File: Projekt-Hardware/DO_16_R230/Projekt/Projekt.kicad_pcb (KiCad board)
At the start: 2 copper layers, 38 parts, among them J1 COM_Bus, J2 COM_Bus, K1 DIPxx-1Cxx-51x, K10 DIPxx-1Cxx-51x, K11 DIPxx-1Cxx-51x, K12 DIPxx-1Cxx-51x, K13 DIPxx-1Cxx-51x, K14 DIPxx-1Cxx-51x, K15 DIPxx-1Cxx-51x, K16 DIPxx-1Cxx-51x, K2 DIPxx-1Cxx-51x, K3 DIPxx-1Cxx-51x, K4 DIPxx-1Cxx-51x, K5 DIPxx-1Cxx-51x, K6 DIPxx-1Cxx-51x, K7 DIPxx-1Cxx-51x, K8 DIPxx-1Cxx-51x, K9 DIPxx-1Cxx-51x, U1 ATmega328P-PU, X1 DO 16-2

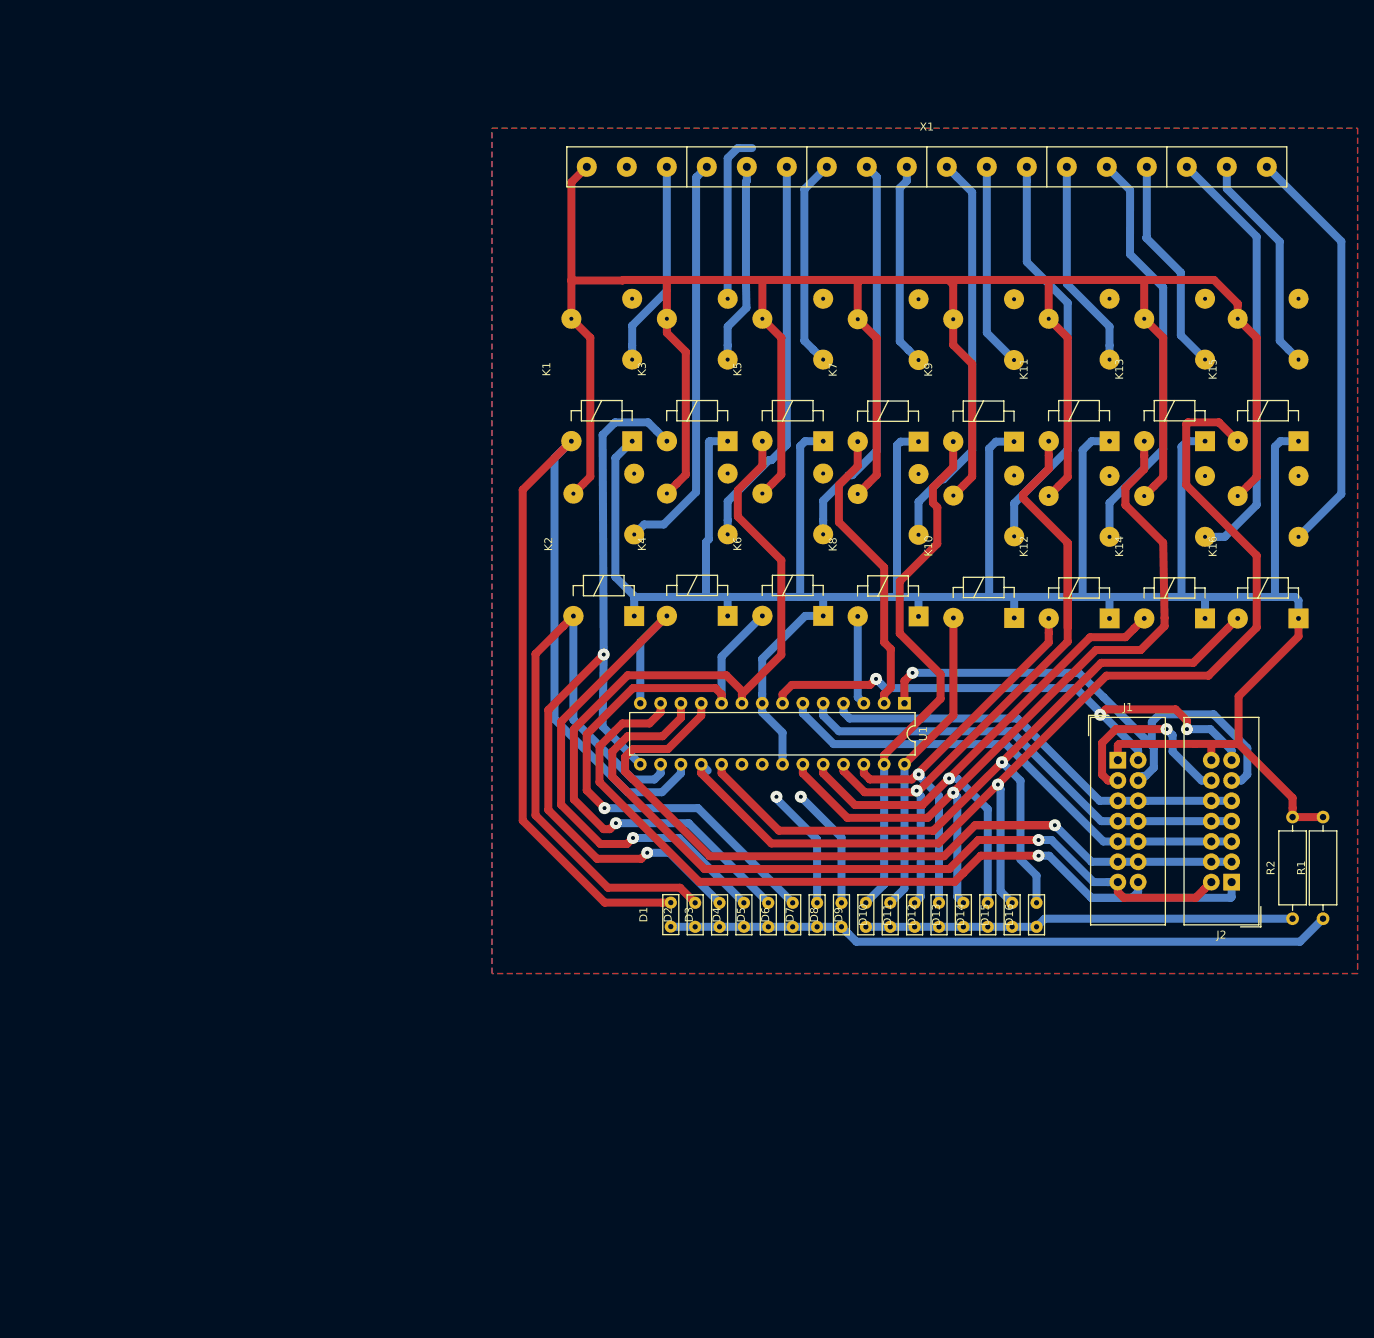
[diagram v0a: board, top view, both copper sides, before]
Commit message: Erster (meschanischer) Entwurf für DO_16_R230 Modul
Erster Entwurf für meschanische Bauteile des
DO_16_R230 Moduls:
- Entwurf für Leiterplatten
Fehlende Entwürfe:
- Gehäuse
- Halterungen
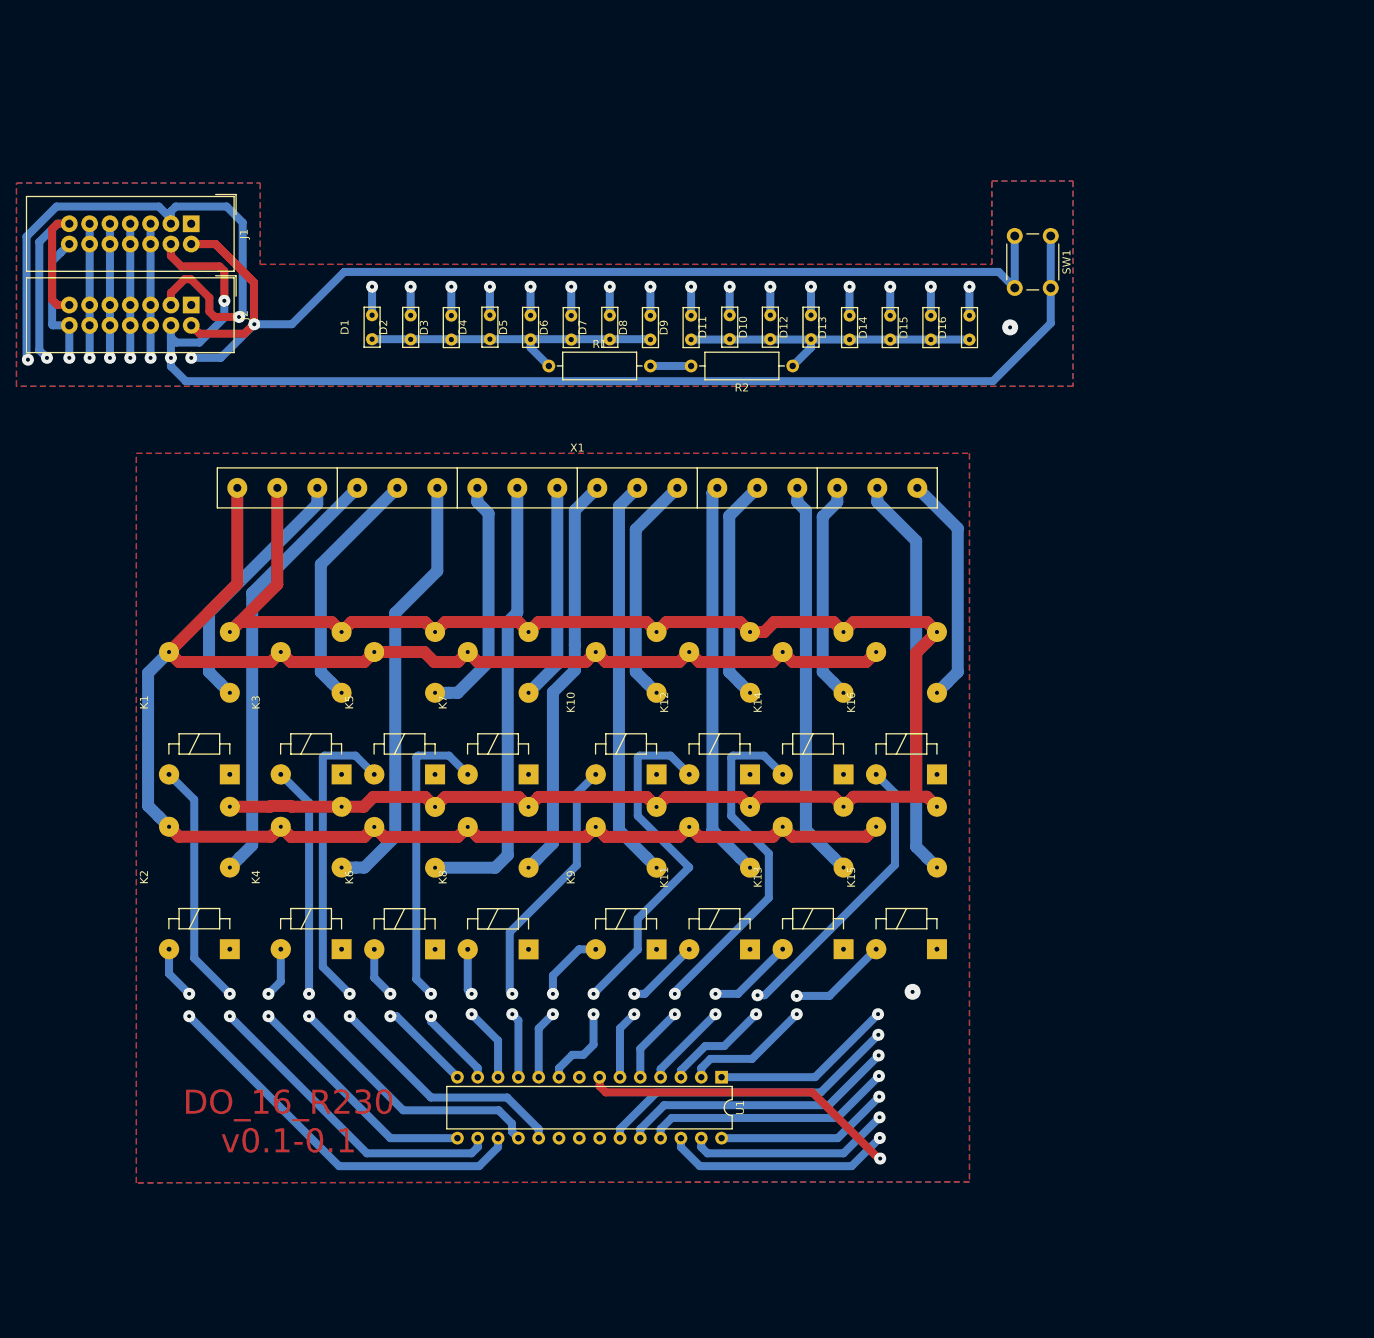
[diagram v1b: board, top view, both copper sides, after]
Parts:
- added SW1: RESET, Button_Switch_THT:SW_PUSH_6mm_H8mm, F.Cu at (171.7, 52.1)
- moved J2 148.7 mm to (64.3, 60.7), turned to 270 degrees
- moved J1 133.8 mm to (64.3, 50.5), turned to 270 degrees
- moved R1 118.9 mm to (109.0, 68.3), turned to 0 degrees
- moved R2 93.2 mm to (139.4, 68.3), turned to 180 degrees
- moved D1 82.4 mm to (86.9, 63.5)
- moved D2 81.6 mm to (91.7, 63.5)
- moved D3 80.7 mm to (96.8, 63.5)
- moved D4 80.0 mm to (101.6, 63.5)
- moved D5 79.2 mm to (106.7, 63.5)
- moved D6 78.5 mm to (111.8, 63.5)
- moved K13 77.9 mm to (145.8, 141.2)
- moved K15 77.9 mm to (157.5, 141.2)
- moved D7 77.9 mm to (116.6, 63.5)
- moved K11 77.8 mm to (134.1, 141.2)
- moved K9 77.6 mm to (122.4, 141.2)
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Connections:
- J2 pad 1: Net-(J1-Pad14) -> Net-(J1-Pad1)
- J2 pad 10: Net-(J1-Pad5) -> Net-(J1-Pad10)
- J2 pad 11: Net-(J1-Pad4) -> Net-(J1-Pad11)
- J2 pad 12: Net-(J1-Pad3) -> Net-(J1-Pad11)
- J2 pad 13: Net-(J1-Pad2) -> Net-(J1-Pad13)
- J2 pad 14: Net-(J1-Pad1) -> Net-(J1-Pad14)
- J2 pad 2: Net-(J1-Pad13) -> Net-(J1-Pad2)
- J2 pad 3: Net-(J1-Pad11) -> Net-(J1-Pad3)
- J2 pad 4: Net-(J1-Pad11) -> Net-(J1-Pad4)
- J2 pad 5: Net-(J1-Pad10) -> Net-(J1-Pad5)
- J2 pad 6: Net-(J1-Pad10) -> Net-(J1-Pad5)
- J2 pad 9: Net-(J1-Pad5) -> Net-(J1-Pad10)
- U1 pad 10: Net-(D6-Pad2) -> Net-(D8-Pad2)
- U1 pad 11: Net-(J1-Pad11) -> Net-(D14-Pad2)
- U1 pad 12: Net-(J1-Pad13) -> Net-(D15-Pad2)
- U1 pad 13: Net-(J1-Pad14) -> Net-(D16-Pad2)
- U1 pad 14: Net-(D4-Pad2) -> Net-(D1-Pad2)
- U1 pad 15: Net-(D3-Pad2) -> Net-(D2-Pad2)
- U1 pad 16: Net-(D2-Pad2) -> Net-(D3-Pad2)
- U1 pad 17: Net-(D1-Pad2) -> Net-(D4-Pad2)
- U1 pad 18: Net-(D15-Pad2) -> Net-(D5-Pad2)
- U1 pad 19: Net-(D16-Pad2) -> Net-(D6-Pad2)
- U1 pad 2: Net-(D7-Pad2) -> Net-(D9-Pad2)
- U1 pad 23: Net-(D13-Pad2) -> Net-(J1-Pad10)
- U1 pad 24: Net-(D14-Pad2) -> Net-(J1-Pad11)
- U1 pad 25: Net-(D11-Pad2) -> Net-(J1-Pad5)
- U1 pad 26: Net-(D12-Pad2) -> Net-(J1-Pad7)
- U1 pad 27: Net-(D9-Pad2) -> Net-(J1-Pad13)
- U1 pad 28: Net-(D10-Pad2) -> Net-(J1-Pad14)
- U1 pad 3: Net-(D8-Pad2) -> Net-(D10-Pad2)
- U1 pad 4: Net-(J1-Pad5) -> Net-(D11-Pad2)
- U1 pad 5: Net-(J1-Pad7) -> Net-(D12-Pad2)
- U1 pad 6: Net-(J1-Pad10) -> Net-(D13-Pad2)
- U1 pad 9: Net-(D5-Pad2) -> Net-(D7-Pad2)
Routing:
- net Net-(J1-Pad1): track 357.0 -> 5.08 mm, vias 0 -> 2
- net Net-(K1-Pad14): track 21.1 -> 232.5 mm
- net Net-(J1-Pad2): track 72.0 -> 193.5 mm
- net Net-(D15-Pad2): track 138.7 -> 25.2 mm, vias 1 -> 3
- net Net-(J1-Pad4): track 66.8 -> 177.1 mm, vias 1 -> 3
- net Net-(K1-Pad1): track 327.5 -> 239.4 mm
- net Net-(D1-Pad2): track 130.0 -> 45.7 mm, vias 0 -> 3
- net Net-(D13-Pad2): track 98.9 -> 22.9 mm, vias 1 -> 3
- net Net-(J1-Pad14): track 112.3 -> 39.1 mm, vias 1 -> 2
- net Net-(D11-Pad2): track 91.4 -> 23.5 mm, vias 1 -> 3
- net Net-(J1-Pad11): track 108.4 -> 51.5 mm, vias 1 -> 2
- net Net-(J1-Pad3): track 24.5 -> 73.6 mm, vias 1 -> 2
- net Net-(D16-Pad2): track 99.0 -> 49.9 mm, vias 1 -> 3
- net Net-(D1-Pad1): track 83.5 -> 39.1 mm
- net Net-(J1-Pad13): track 101.0 -> 58.9 mm, vias 1 -> 2
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- added copper zone on B.Cu, net Net-(J1-Pad1)
- added copper zone on F.Cu, net Net-(J1-Pad1)
- removed copper zone on F.Cu, net (none)
- removed copper zone on B.Cu, net Net-(K1-Pad14)
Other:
- board text added: "DO_16_R230 v0.1-0.1"

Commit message: Gehäuse für DO_16_R230 begonnen
Angefangen Gehäuse für DO_16_R230
angefangen zu entwerfen.
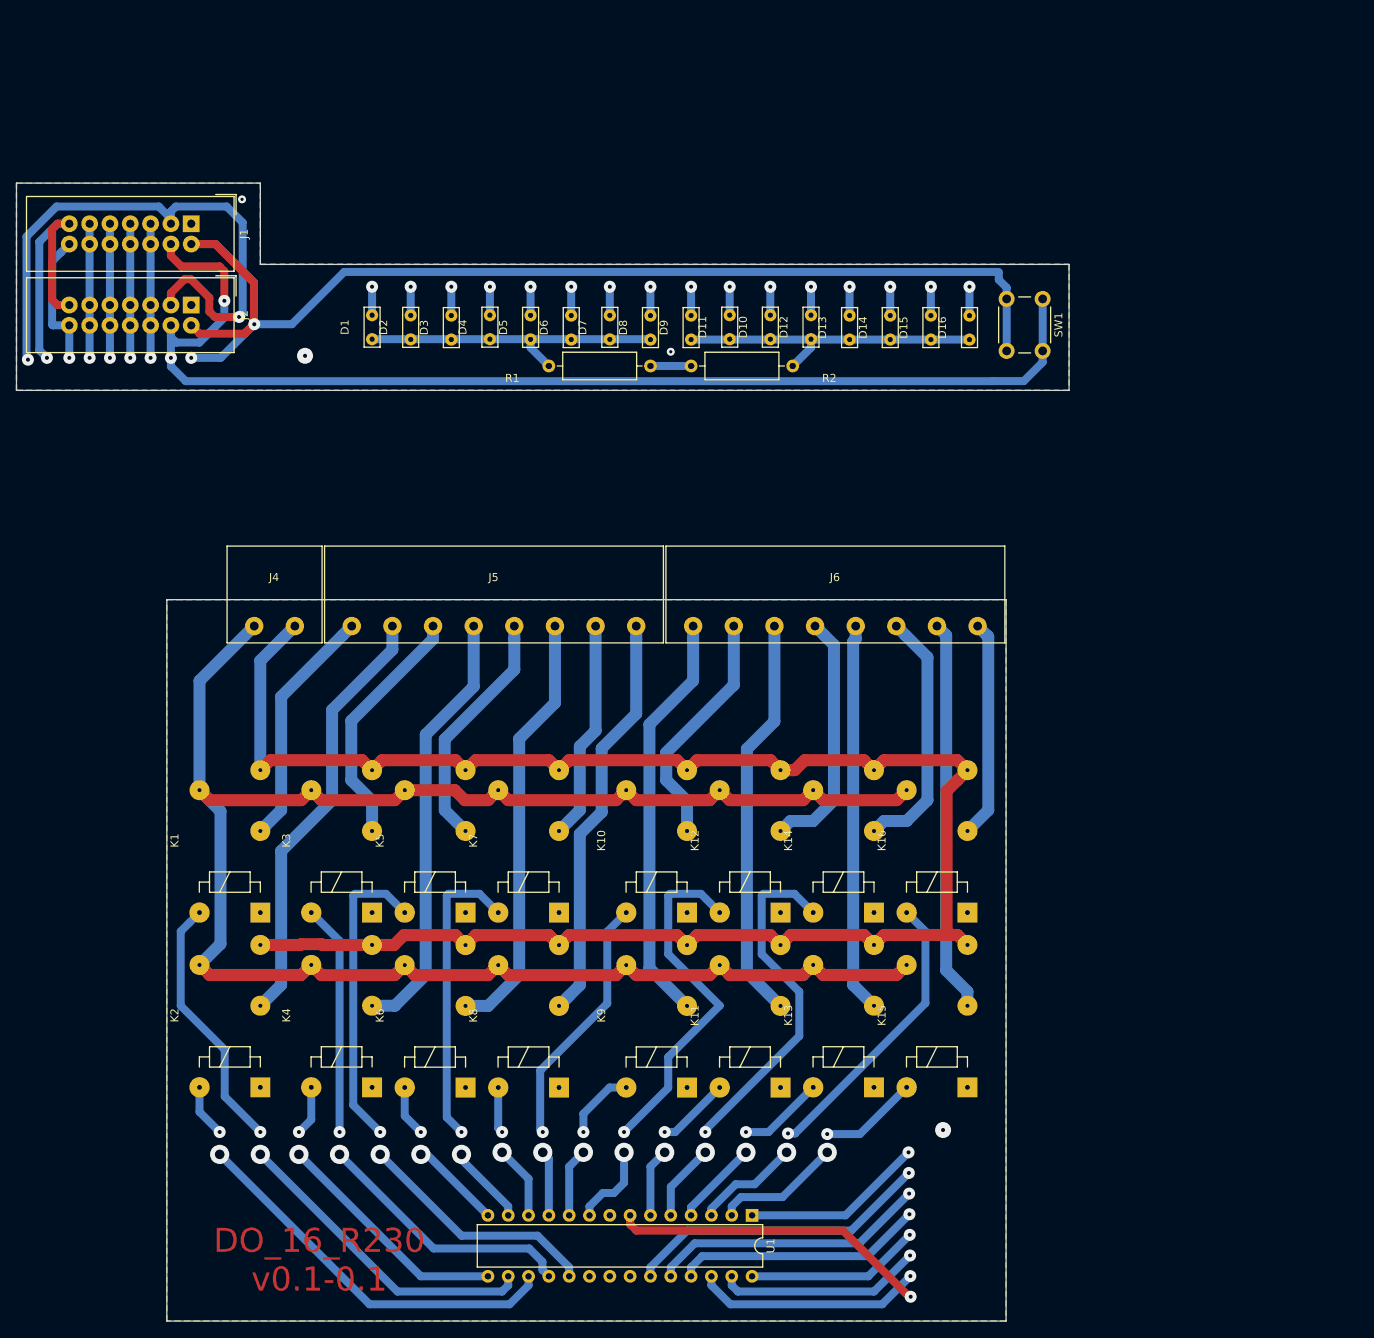
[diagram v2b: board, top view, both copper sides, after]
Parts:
- removed X1: DO 16-2, Footprints:Klemmleiste_R5mm_B8mm_Kopie
- added J4: Conn_01x02, Footprints:RND_Steckklemme_2, F.Cu at (74.7, 95.8)
- added J5: Conn_01x08, Footprints:RND_Steckklemme_8, F.Cu at (102.1, 95.8)
- added J6: Conn_01x08, Footprints:RND_Steckklemme_8, F.Cu at (144.8, 95.8)
- moved K13 17.7 mm to (149.6, 158.5)
- moved K15 17.7 mm to (161.3, 158.5)
- moved K2 17.7 mm to (72.9, 158.5)
- moved K4 17.7 mm to (86.9, 158.5)
- moved K1 17.7 mm to (72.9, 136.7)
- moved K10 17.7 mm to (126.2, 136.7)
- moved K11 17.7 mm to (137.9, 158.5)
- moved K12 17.7 mm to (137.9, 136.7)
- moved K14 17.7 mm to (149.6, 136.7)
- moved K16 17.7 mm to (161.3, 136.7)
- moved K5 17.7 mm to (98.6, 136.7)
- moved K6 17.7 mm to (98.6, 158.5)
- moved K7 17.7 mm to (110.2, 136.7)
- moved K8 17.7 mm to (110.2, 158.5)
- moved K9 17.7 mm to (126.2, 158.5)
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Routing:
- net Net-(J1-Pad4): track 177.1 -> 171.1 mm
- net Net-(J6-Pad6): track 27.4 -> 31.7 mm
- net Net-(J6-Pad4): track 28.1 -> 31.0 mm
- net Net-(J5-Pad6): track 56.1 -> 53.8 mm
- net Net-(J5-Pad1): track 32.3 -> 30.3 mm
- net Net-(D1-Pad2): track 45.7 -> 47.6 mm
- net Net-(J6-Pad8): track 28.8 -> 27.2 mm
- net Net-(J6-Pad7): track 50.5 -> 49.0 mm
- net Net-(J6-Pad2): track 28.8 -> 30.2 mm
- net Net-(J6-Pad1): track 50.4 -> 51.7 mm
- net Net-(J6-Pad5): track 49.8 -> 48.7 mm
- net Net-(J6-Pad3): track 49.7 -> 50.6 mm
- net Net-(J1-Pad2): track 193.5 -> 194.2 mm
- net Net-(J4-Pad1): track 239.4 -> 238.7 mm
- net Net-(J4-Pad2): track 232.5 -> 231.8 mm
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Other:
- board outline added: 131.6 x 142.2 mm

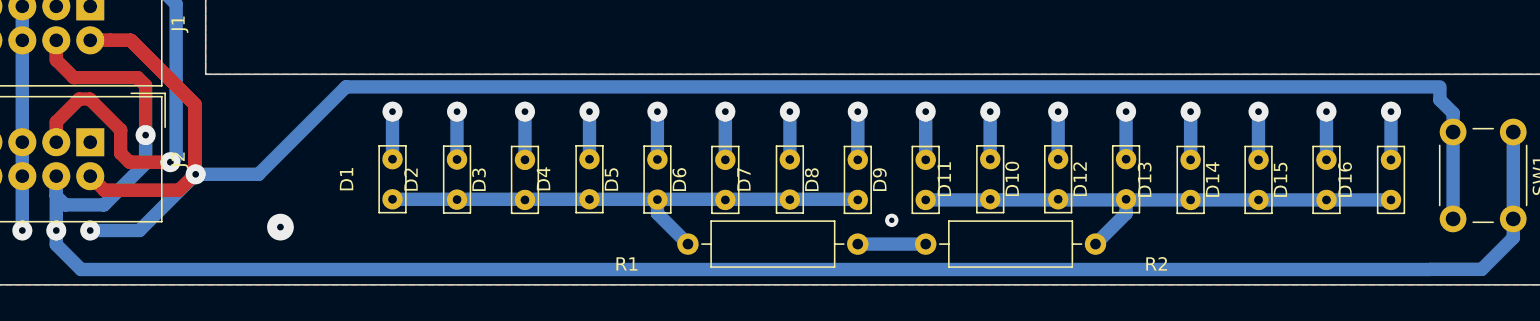
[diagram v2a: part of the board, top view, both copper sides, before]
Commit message: Korrektur im Schaltplan
RESET Taster auf von +5V auf GND verschoben.
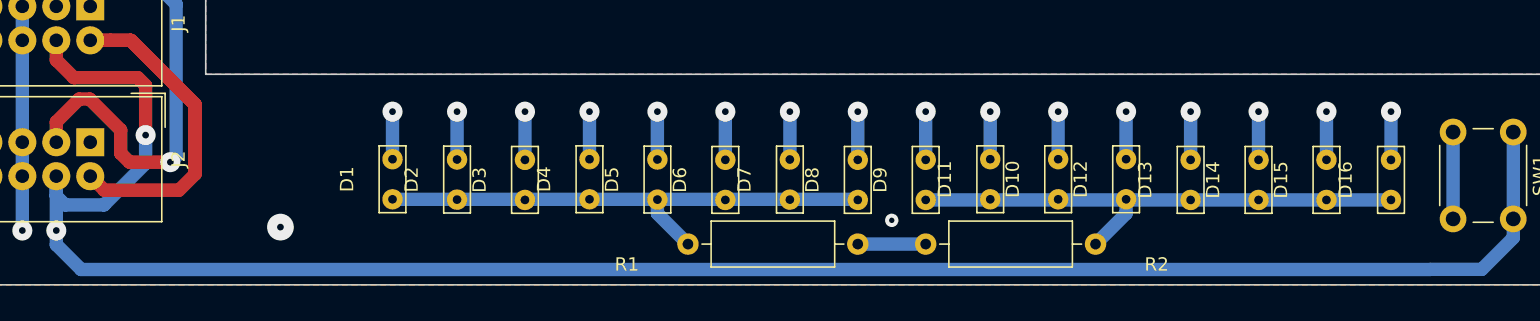
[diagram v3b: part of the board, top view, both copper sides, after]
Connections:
- SW1 pad 2: Net-(J1-Pad2) -> Net-(J1-Pad1)
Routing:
- net Net-(J1-Pad2): track 194.2 -> 78.8 mm, vias 3 -> 1
- net Net-(J1-Pad1): track 5.08 -> 11.6 mm
